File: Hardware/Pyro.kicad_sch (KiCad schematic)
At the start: 47 parts, among them J12 Conn_01x02_Male, Q2 BUK9M11-40EX, Q5 BSZ025N04LS, Q6 BSZ025N04LS, U10 SiC437BED-T1-GE3, U11 LM74810, U12 INA219AxDCN, U9 782-TCMT1109

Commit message: Almost done
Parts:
- removed R108, R94: 3.3k, Resistor_SMD:R_0402_1005Metric, symbol Device:R_Small
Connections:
- net BUS_VMON renamed PyroVMON

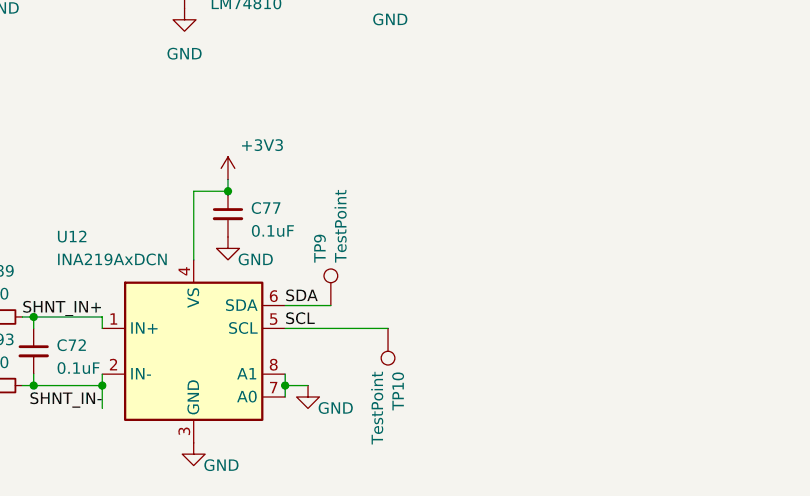
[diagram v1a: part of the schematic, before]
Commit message: Fixed all DRC Errors
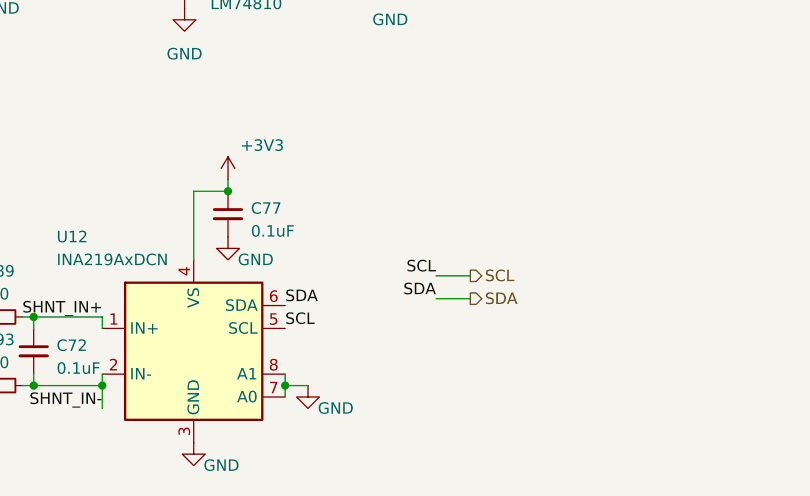
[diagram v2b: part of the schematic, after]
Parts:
- removed TP10, TP9: TestPoint, TestPoint:TestPoint_Pad_D1.0mm, symbol Connector:TestPoint
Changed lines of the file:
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@@
 	(wire
 		(pts
-			(xy 96.012 177.546) (xy 107.442 177.546)
-		)
-		(stroke
-			(width 0)
-			(type default)
-		)
-	)
-	(wire
-		(pts
 			(xy 187.706 65.532) (xy 204.724 65.532)
 		)
@@
 	(wire
 		(pts
-			(xy 96.012 175.006) (xy 101.092 175.006)
-		)
-		(stroke
-			(width 0)
-			(type default)
-		)
-	)
-	(wire
-		(pts
 			(xy 192.278 42.672) (xy 204.724 42.672)
 		)
@@
 	(wire
 		(pts
+			(xy 116.586 171.704) (xy 112.776 171.704)
+		)
+		(stroke
+			(width 0)
+			(type default)
+		)
+	)
+	(wire
+		(pts
 			(xy 188.214 52.832) (xy 193.294 52.832)
 		)
@@
 	(wire
 		(pts
+			(xy 116.586 174.244) (xy 112.776 174.244)
+		)
+		(stroke
+			(width 0)
+			(type default)
+		)
+	)
+	(wire
+		(pts
 			(xy 96.012 183.896) (xy 96.012 185.166)
 		)
@@
 		)
 	)
+	(label "SCL"
+		(at 112.776 171.704 180)
+		(effects
+			(font
+				(size 1.27 1.27)
+			)
+			(justify right bottom)
+		)
+	)
 	(label "HGate"
 		(at 102.616 115.316 90)
@@
 	)
 	(label "SDA"
+		(at 112.776 174.244 180)
+		(effects
+			(font
+				(size 1.27 1.27)
+			)
+			(justify right bottom)
+		)
+	)
+	(label "SDA"
 		(at 96.012 175.006 0)
 		(effects
@@
 		)
 	)
+	(hierarchical_label "SDA"
+		(shape output)
+		(at 116.586 174.244 0)
+		(effects
+			(font
+				(size 1.27 1.27)
+			)
+			(justify left)
+		)
+	)
 	(hierarchical_label "Cont1"
 		(shape output)
@@
 		)
 	)
+	(hierarchical_label "SCL"
+		(shape output)
+		(at 116.586 171.704 0)
+		(effects
+			(font
+				(size 1.27 1.27)
+			)
+			(justify left)
+		)
+	)
 	(hierarchical_label "Nuke 1"
 		(shape input)
@@
 	)
 	(symbol
-		(lib_id "Connector:TestPoint")
-		(at 107.442 177.546 180)
-		(unit 1)
-		(exclude_from_sim no)
-		(in_bom yes)
-		(on_board yes)
-		(dnp no)
-		(property "Reference" "TP10"
-			(at 108.6104 182.3212 90)
-			(effects
-				(font
-					(size 1.27 1.27)
-				)
-				(justify left)
-			)
-		)
-		(property "Value" "TestPoint"
-			(at 106.299 182.3212 90)
-			(effects
-				(font
-					(size 1.27 1.27)
-				)
-				(justify left)
-			)
-		)
-		(property "Footprint" "TestPoint:TestPoint_Pad_D1.0mm"
-			(at 102.362 177.546 0)
-			(effects
-				(font
-					(size 1.27 1.27)
-				)
-				(hide yes)
-			)
-		)
-		(property "Datasheet" "~"
-			(at 102.362 177.546 0)
-			(effects
-				(font
-					(size 1.27 1.27)
-				)
-				(hide yes)
-			)
-		)
-		(property "Description" ""
-			(at 107.442 177.546 0)
-			(effects
-				(font
-					(size 1.27 1.27)
-				)
-				(hide yes)
-			)
-		)
-		(pin "1"
-		)
-		(instances
-			(project "Ricardo-Stark"
-				(path "/7db990e4-92e1-4f99-b4d2-435bbec1ba83/3c6662b6-8783-49dc-b944-3dc2b3e30a07"
-					(reference "TP10")
-					(unit 1)
-				)
-			)
-		)
-	)
-	(symbol
 		(lib_id "power:GND")
 		(at 44.196 124.206 0)
@@
 					(unit 1)
 				)
-			)
-		)
-	)
-	(symbol
-		(lib_id "Connector:TestPoint")
-		(at 101.092 175.006 0)
-		(unit 1)
-		(exclude_from_sim no)
-		(in_bom yes)
-		(on_board yes)
-		(dnp no)
-		(property "Reference" "TP9"
-			(at 99.9236 170.2308 90)
-			(effects
-				(font
-					(size 1.27 1.27)
-				)
-				(justify left)
-			)
-		)
-		(property "Value" "TestPoint"
-			(at 102.235 170.2308 90)
-			(effects
-				(font
-					(size 1.27 1.27)
-				)
-				(justify left)
-			)
-		)
-		(property "Footprint" "TestPoint:TestPoint_Pad_D1.0mm"
-			(at 106.172 175.006 0)
-			(effects
-				(font
-					(size 1.27 1.27)
-				)
-				(hide yes)
-			)
-		)
-		(property "Datasheet" "~"
-			(at 106.172 175.006 0)
-			(effects
-				(font
-					(size 1.27 1.27)
-				)
-				(hide yes)
-			)
-		)
-		(property "Description" ""
-			(at 101.092 175.006 0)
-			(effects
-				(font
-					(size 1.27 1.27)
-				)
-				(hide yes)
-			)
-		)
-		(pin "1"
-		)
-		(instances
-			(project "Ricardo-Stark"
-				(path "/7db990e4-92e1-4f99-b4d2-435bbec1ba83/3c6662b6-8783-49dc-b944-3dc2b3e30a07"
-					(reference "TP9")
-					(unit 1)
-				)

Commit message: Most Review Changes
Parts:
- removed D19: P6SMBJ28CA, Diode_SMD:D_SMA, symbol Device:D_TVS_Small_Filled
- removed Q2: BUK9M11-40EX, Package_TO_SOT_SMD:LFPAK33, symbol Transistor_FET:BUK9M11-40EX
- added Q7: BSZ025N04LS, iclr:BSZ025N04LS, symbol iclr:BSZ025N04LS
- added R14: 4.7k, Resistor_SMD:R_0402_1005Metric, symbol Device:R_Small
- added R94: 4.7k, Resistor_SMD:R_0402_1005Metric, symbol Device:R
- R11: value 10k -> 4.7k
- U10: value SiC437BED-T1-GE3 -> SiC438BED-T1-GE3
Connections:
- net GND: now also Q7.1 (S), Q7.2 (S), Q7.3 (S), Q7.A1 (S), R14.1, R94.2
- net Nuke 1: now also Q7.4 (G), R94.1
- net PyroV: now also R14.2
- net at D3.3 (K): now also Q7.5 (D), Q7.6 (D), Q7.7 (D), Q7.8 (D), Q7.A5 (D)
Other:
- note removed: "Batt Mon - 3.0V out @ 35V in Overvoltage cutoff - 32V Check sizing script"
- note removed: "LTV 247 is a single chip represented by multiple smaller chips"
- moved on the sheet: D3, D4, D9, Firing1, J12, R77, R79, U9A

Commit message: Remaining Review Changes
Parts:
- R14: value 4.7k -> 10k
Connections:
- net PyroVMON: no longer names the net of R44.2, R71.2
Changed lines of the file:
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@@
 	)
 	(junction
-		(at 107.696 128.016)
-		(diameter 0)
-		(color 0 0 0 0)
-	)
-	(junction
 		(at 102.616 66.294)
 		(diameter 0)
@@
 	(wire
 		(pts
-			(xy 126.746 128.016) (xy 107.696 128.016)
-		)
-		(stroke
-			(width 0)
-			(type default)
-		)
-	)
-	(wire
-		(pts
 			(xy 74.168 80.01) (xy 77.216 80.01)
 		)
@@
 		)
 	)
-	(hierarchical_label "PyroVMON"
-		(shape output)
-		(at 126.746 128.016 0)
-		(effects
-			(font
-				(size 1.27 1.27)
-			)
-			(justify left)
-		)
-	)
 	(hierarchical_label "SCL"
 		(shape output)
@@
 			)
 		)
-		(property "Value" "4.7k"
+		(property "Value" "10k"
 			(at 68.326 188.976 0)
 			(effects

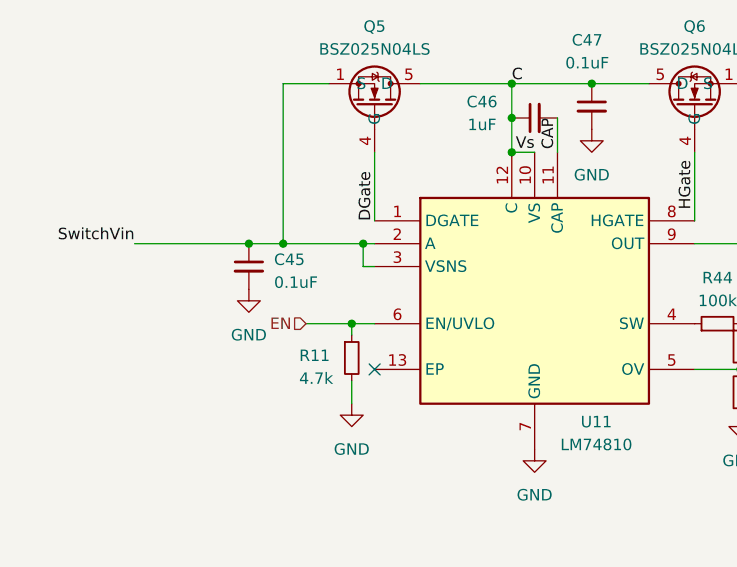
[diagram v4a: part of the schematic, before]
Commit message: Forgot switch enable DNP pull up
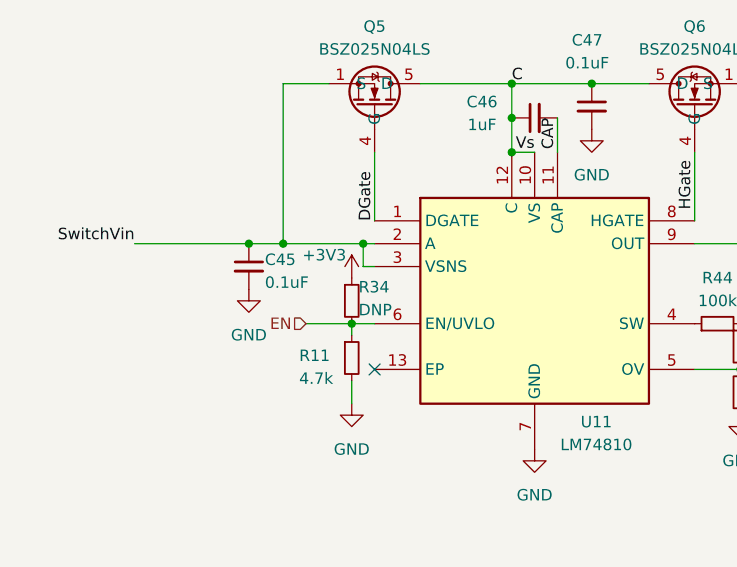
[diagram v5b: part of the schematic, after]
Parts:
- added R34: DNP, Resistor_SMD:R_0402_1005Metric, symbol Device:R_Small
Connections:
- net +3V3: now also R34.1
- net EN: now also R34.2
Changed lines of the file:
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@@
+	)
+	(symbol
+		(lib_id "power:+3.3V")
+		(at 64.516 122.936 0)
+		(unit 1)
+		(exclude_from_sim no)
+		(in_bom yes)
+		(on_board yes)
+		(dnp no)
+		(property "Reference" "#PWR0208"
+			(at 64.516 126.746 0)
+			(effects
+				(font
+					(size 1.27 1.27)
+				)
+				(hide yes)
+			)
+		)
+		(property "Value" "+3V3"
+			(at 61.468 120.396 0)
+			(effects
+				(font
+					(size 1.27 1.27)
+				)
+			)
+		)
+		(property "Footprint" ""
+			(at 64.516 122.936 0)
+			(effects
+				(font
+					(size 1.27 1.27)
+				)
+				(hide yes)
+			)
+		)
+		(property "Datasheet" ""
+			(at 64.516 122.936 0)
+			(effects
+				(font
+					(size 1.27 1.27)
+				)
+				(hide yes)
+			)
+		)
+		(property "Description" ""
+			(at 64.516 122.936 0)
+			(effects
+				(font
+					(size 1.27 1.27)
+				)
+				(hide yes)
+			)
+		)
+		(pin "1"
+		)
+		(instances
+			(project "Ricardo-Stark"
+				(path "/7db990e4-92e1-4f99-b4d2-435bbec1ba83/3c6662b6-8783-49dc-b944-3dc2b3e30a07"
+					(reference "#PWR0208")
+					(unit 1)
+				)
+			)
+		)
 	)
 	(symbol
@@
 	)
 	(symbol
+		(lib_id "Device:R_Small")
+		(at 64.516 125.476 0)
+		(unit 1)
+		(exclude_from_sim no)
+		(in_bom yes)
+		(on_board yes)
+		(dnp no)
+		(property "Reference" "R34"
+			(at 65.278 123.952 0)
+			(effects
+				(font
+					(size 1.27 1.27)
+				)
+				(justify left)
+			)
+		)
+		(property "Value" "DNP"
+			(at 65.278 126.492 0)
+			(effects
+				(font
+					(size 1.27 1.27)
+				)
+				(justify left)
+			)
+		)
+		(property "Footprint" "Resistor_SMD:R_0402_1005Metric"
+			(at 64.516 125.476 0)
+			(effects
+				(font
+					(size 1.27 1.27)
+				)
+				(hide yes)
+			)
+		)
+		(property "Datasheet" "~"
+			(at 64.516 125.476 0)
+			(effects
+				(font
+					(size 1.27 1.27)
+				)
+				(hide yes)
+			)
+		)
+		(property "Description" "Resistor, small symbol"
+			(at 64.516 125.476 0)
+			(effects
+				(font
+					(size 1.27 1.27)
+				)
+				(hide yes)
+			)
+		)
+		(pin "1"
+		)
+		(pin "2"
+		)
+		(instances
+			(project "Ricardo-Stark"
+				(path "/7db990e4-92e1-4f99-b4d2-435bbec1ba83/3c6662b6-8783-49dc-b944-3dc2b3e30a07"
+					(reference "R34")
+					(unit 1)
+				)
+			)
+		)
+	)
+	(symbol
 		(lib_id "Device:LED")
 		(at 77.216 66.294 90)
@@
 		(dnp no)
 		(property "Reference" "C45"
-			(at 55.88 120.904 0)
+			(at 54.864 120.904 0)
 			(effects
 				(font
@@
 		)
 		(property "Value" "0.1uF"
-			(at 55.88 123.444 0)
-			(effects
-				(font
+			(at 54.864 123.444 0)
+			(effects
+				(font

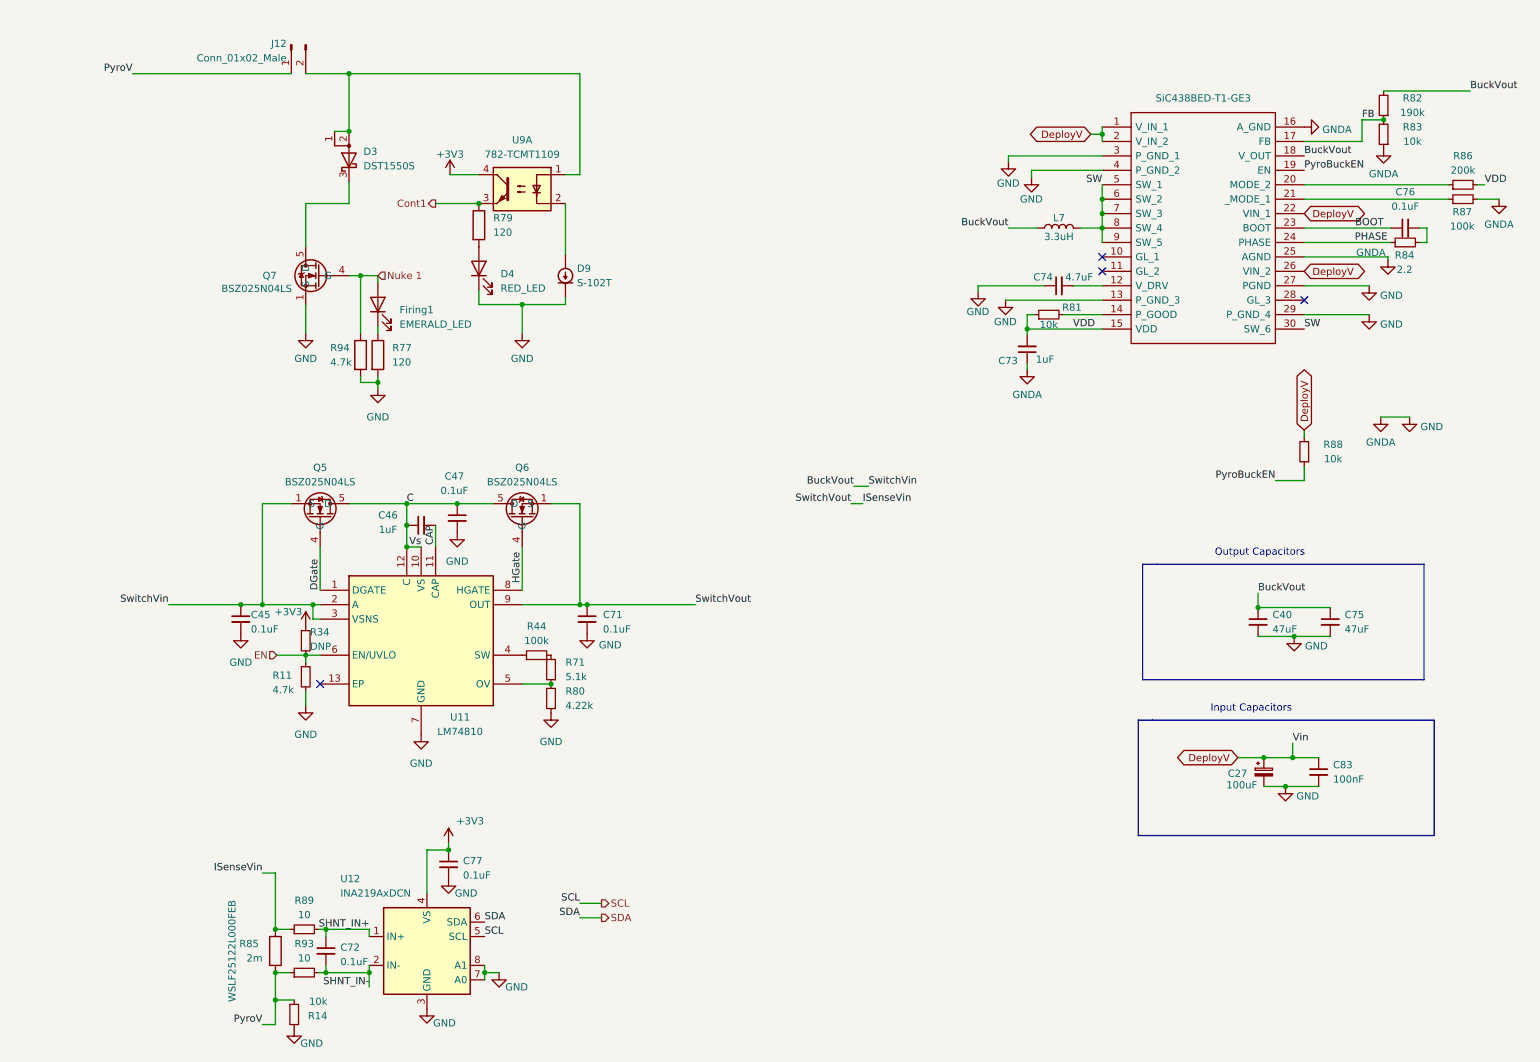
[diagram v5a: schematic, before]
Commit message: Replaced PicoClasp with nanofits
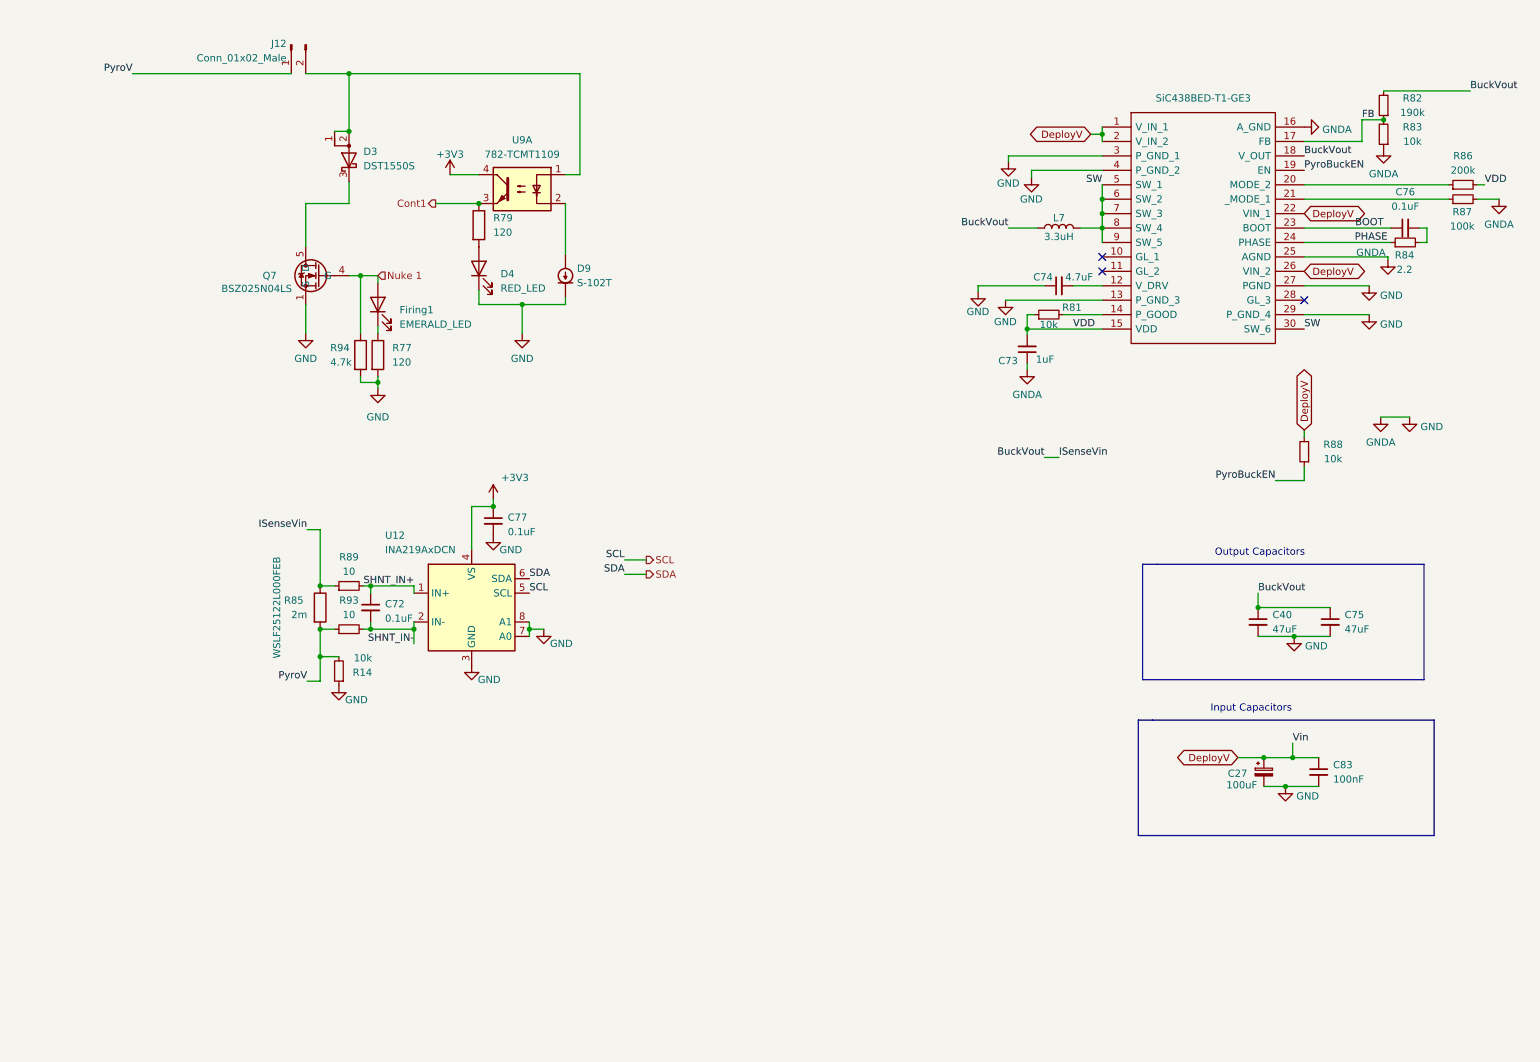
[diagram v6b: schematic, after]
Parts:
- removed C45, C71: 0.1uF, Capacitor_SMD:C_0402_1005Metric, symbol Device:C_Small
- removed C46: 1uF, Capacitor_SMD:C_0402_1005Metric, symbol Device:C_Small
- removed C47: 0.1uF, Capacitor_SMD:C_0603_1608Metric, symbol Device:C_Small
- removed Q5, Q6: BSZ025N04LS, iclr:BSZ025N04LS, symbol iclr:BSZ025N04LS
- removed R11: 4.7k, Resistor_SMD:R_0402_1005Metric, symbol Device:R_Small
- removed R34: DNP, Resistor_SMD:R_0402_1005Metric, symbol Device:R_Small
- removed R44: 100k, Resistor_SMD:R_0402_1005Metric, symbol Device:R_Small
- removed R71: 5.1k, Resistor_SMD:R_0402_1005Metric, symbol Device:R_Small
- removed R80: 4.22k, Resistor_SMD:R_0402_1005Metric, symbol Device:R_Small
- removed U11: LM74810, iclr:SON50P300X300X80-13N-D, symbol iclr:LM74810QDRRRQ1
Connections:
- net ISenseVin is gone; now on net BuckVout: R85.1, R89.1
- no-connect marks 4 -> 3
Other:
- moved on the sheet: C72, C77, R14, R85, R89, R93, U12

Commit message: Solenoid Feature and minor changes
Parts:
- added C46, C47, C71, C91, C92: 47uF, Capacitor_SMD:C_1206_3216Metric, symbol Device:C_Small
- added D10, D13: S-102T, iclr:SODFL3516X70N, symbol Device:D_Current-regulator
- added D11, D5: DST1550S, Package_TO_SOT_SMD:TO-277B, symbol Device:D_Schottky_AAK
- added D12, D8: RED_LED, LED_SMD:LED_0603_1608Metric, symbol Device:LED
- added D16, D17: V8PAM10S-M3/I, iclr:V8PAM10SM3I, symbol Device:D_Schottky_Small_Filled
- added Firing2, Firing3: EMERALD_LED, LED_SMD:LED_0402_1005Metric, symbol Device:LED
- added J14, J15: Conn_01x02_Male, Connector_Molex:Molex_Nano-Fit_105313-xx02_1x02_P2.50mm_Horizontal, symbol Connector:Conn_01x02_Male
- added Q8, Q9: BSZ025N04LS, iclr:BSZ025N04LS, symbol iclr:BSZ025N04LS
- added R108, R114: 4.7k, Resistor_SMD:R_0402_1005Metric, symbol Device:R
- added R113, R116: 120, Resistor_SMD:R_0603_1608Metric, symbol Device:R
- added R115, R80: 120, Resistor_SMD:R_0402_1005Metric, symbol Device:R
- added U11, U15: 782-TCMT1109, iclr:TCMT1109-4N, symbol Isolator:LTV-247
- R82: footprint Resistor_SMD:R_0402_1005Metric -> Resistor_SMD:R_0603_1608Metric_Pad0.98x0.95mm_HandSolder
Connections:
- net +3V3: now also U11.4, U15.4
- net DeployV: now also C46.1, C47.1, C71.1, C91.1, C92.1, D16.1 (K), D17.1 (K), J14.1 (Pin_1), J15.1 (Pin_1)
- net GND: now also C46.2, C47.2, C71.2, C91.2, C92.2, D10.1 (K), D12.1 (K), D13.1 (K), D8.1 (K), Firing2.1 (K), Firing3.1 (K), Q8.1 (S), Q8.2 (S), Q8.3 (S), Q8.A1 (S), Q9.1 (S), Q9.2 (S), Q9.3 (S), Q9.A1 (S), R108.2, R114.2
- new net: D8.2 (A), R113.2
- new net: D11.1 (A), D11.2 (A), D17.2 (A), J15.2 (Pin_2), U15.1
- new net: D11.3 (K), Q9.5 (D), Q9.6 (D), Q9.7 (D), Q9.8 (D), Q9.A5 (D)
- new net: D16.2 (A), D5.1 (A), D5.2 (A), J14.2 (Pin_2), U11.1
- new net: D10.2 (A), U11.2
- new net: D13.2 (A), U15.2
- new net: D5.3 (K), Q8.5 (D), Q8.6 (D), Q8.7 (D), Q8.8 (D), Q8.A5 (D)
- new net: Firing2.2 (A), R80.2
- new net: D12.2 (A), R116.2
- new net: Firing3.2 (A), R115.2
- new net Cont2: R113.1, U11.3
- new net Cont3: R116.1, U15.3
- new net Nuke 2: Q8.4 (G), R108.1, R80.1
- new net Nuke 3: Q9.4 (G), R114.1, R115.1
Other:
- moved on the sheet: C27, C40, C72, C73, C74, C75, C76, C77, C83, D3, D4, D9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

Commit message: Review Changes
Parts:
- removed C92: 47uF, Capacitor_SMD:C_1206_3216Metric, symbol Device:C_Small
- added F1: 2920L500/24SLDR, Fuse:Fuse_2920_7451Metric, symbol Device:Polyfuse_Small
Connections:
- net DeployV: now also F1.1; no longer C91.1, D16.1 (K), D17.1 (K), J14.1 (Pin_1), J15.1 (Pin_1)
- new net Sol_PWR: C91.1, D16.1 (K), D17.1 (K), F1.2, J14.1 (Pin_1), J15.1 (Pin_1)
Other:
- moved on the sheet: C46, C91, D10, D11, D12, D13, D16, D17, D5, D8, Firing2, Firing3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
